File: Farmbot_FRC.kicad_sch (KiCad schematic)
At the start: 0 parts

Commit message: mkb
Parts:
- added J1: XT60-M, XT60-M:AMASS_XT60-M, symbol XT60-M:XT60-M
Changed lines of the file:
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@@
 	(generator_version "9.0")
 	(paper "A4")
+	(symbol
+		(lib_id "XT60-M:XT60-M")
+		(at 59.182 26.162 0)
+		(unit 1)
+		(exclude_from_sim no)
+		(in_bom yes)
+		(on_board yes)
+		(dnp no)
+		(fields_autoplaced yes)
+		(property "Reference" "J1"
+			(at 68.58 23.6219 0)
+			(effects
+				(font
+					(size 1.27 1.27)
+				)
+				(justify left)
+			)
+		)
+		(property "Value" "XT60-M"
+			(at 68.58 26.1619 0)
+			(effects
+				(font
+					(size 1.27 1.27)
+				)
+				(justify left)
+			)
+		)
+		(property "Footprint" "XT60-M:AMASS_XT60-M"
+			(at 59.182 26.162 0)
+			(effects
+				(font
+					(size 1.27 1.27)
+				)
+				(justify bottom)
+				(hide yes)
+			)
+		)
+		(property "Datasheet" ""
+			(at 59.182 26.162 0)
+			(effects
+				(font
+					(size 1.27 1.27)
+				)
+				(hide yes)
+			)
+		)
+		(property "Description" ""
+			(at 59.182 26.162 0)
+			(effects
+				(font
+					(size 1.27 1.27)
+				)
+				(hide yes)
+			)
+		)
+		(property "MF" "AMASS"
+			(at 59.182 26.162 0)
+			(effects
+				(font
+					(size 1.27 1.27)
+				)
+				(justify bottom)
+				(hide yes)
+			)
+		)
+		(property "MAXIMUM_PACKAGE_HEIGHT" "16.00 mm"
+			(at 59.182 26.162 0)
+			(effects
+				(font
+					(size 1.27 1.27)
+				)
+				(justify bottom)
+				(hide yes)
+			)
+		)
+		(property "Package" "Package"
+			(at 59.182 26.162 0)
+			(effects
+				(font
+					(size 1.27 1.27)
+				)
+				(justify bottom)
+				(hide yes)
+			)
+		)
+		(property "Price" "None"
+			(at 59.182 26.162 0)
+			(effects
+				(font
+					(size 1.27 1.27)
+				)
+				(justify bottom)
+				(hide yes)
+			)
+		)
+		(property "Check_prices" "https://www.snapeda.com/parts/XT60-M/AMASS/view-part/?ref=eda"
+			(at 59.182 26.162 0)
+			(effects
+				(font
+					(size 1.27 1.27)
+				)
+				(justify bottom)
+				(hide yes)
+			)
+		)
+		(property "STANDARD" "IPC 7351B"
+			(at 59.182 26.162 0)
+			(effects
+				(font
+					(size 1.27 1.27)
+				)
+				(justify bottom)
+				(hide yes)
+			)
+		)
+		(property "PARTREV" "V1.2"
+			(at 59.182 26.162 0)
+			(effects
+				(font
+					(size 1.27 1.27)
+				)
+				(justify bottom)
+				(hide yes)
+			)
+		)
+		(property "SnapEDA_Link" "https://www.snapeda.com/parts/XT60-M/AMASS/view-part/?ref=snap"
+			(at 59.182 26.162 0)
+			(effects
+				(font
+					(size 1.27 1.27)
+				)
+				(justify bottom)
+				(hide yes)
+			)
+		)
+		(property "MP" "XT60-M"
+			(at 59.182 26.162 0)
+			(effects
+				(font
+					(size 1.27 1.27)
+				)
+				(justify bottom)
+				(hide yes)
+			)
+		)
+		(property "Description_1" "Plug; DC supply; XT60; male; PIN: 2; for cable; soldered; 30A; 500V"
+			(at 59.182 26.162 0)
+			(effects
+				(font
+					(size 1.27 1.27)
+				)
+				(justify bottom)
+				(hide yes)
+			)
+		)
+		(property "Availability" "Not in stock"
+			(at 59.182 26.162 0)
+			(effects
+				(font
+					(size 1.27 1.27)
+				)
+				(justify bottom)
+				(hide yes)
+			)
+		)
+		(property "MANUFACTURER" "AMASS"
+			(at 59.182 26.162 0)
+			(effects
+				(font
+					(size 1.27 1.27)
+				)
+				(justify bottom)
+				(hide yes)
+			)
+		)
+		(pin "P"
+		)
+		(pin "N"
+		)
+		(instances
+			(project ""
+				(path "/c45fa9ee-2918-4f46-896e-3838974ce73e"
+					(reference "J1")
+					(unit 1)
+				)
+			)
+		)
+	)
 	(sheet_instances
 		(path "/"

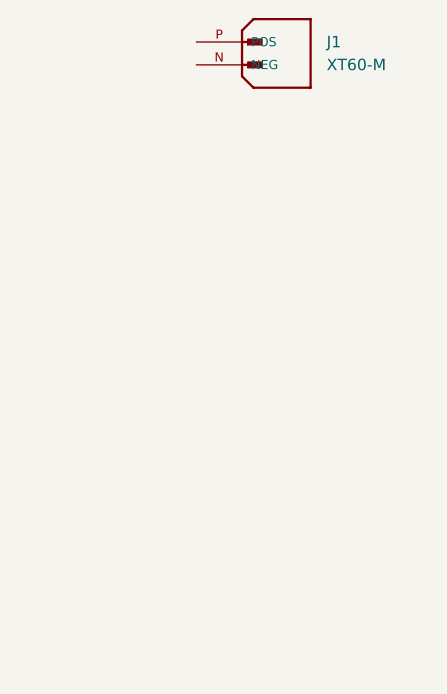
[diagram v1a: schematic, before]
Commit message: added rpi zero
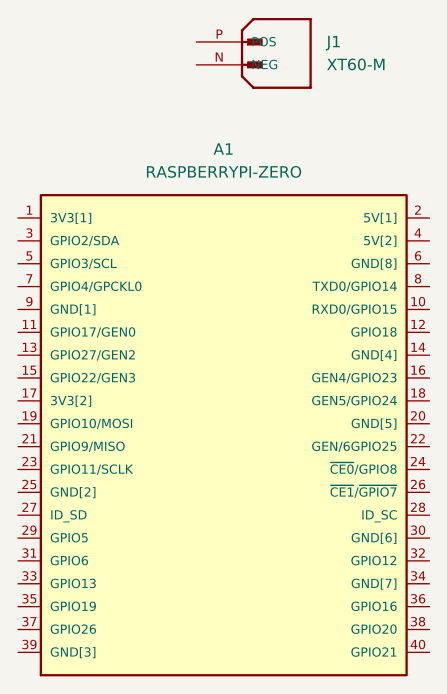
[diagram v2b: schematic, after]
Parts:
- added A1: RASPBERRYPI-ZERO, RASPBERRYPI-ZERO:RASPBERRYPI-ZERO_RPI-ZERO, symbol RASPBERRYPI-ZERO:RASPBERRYPI-ZERO

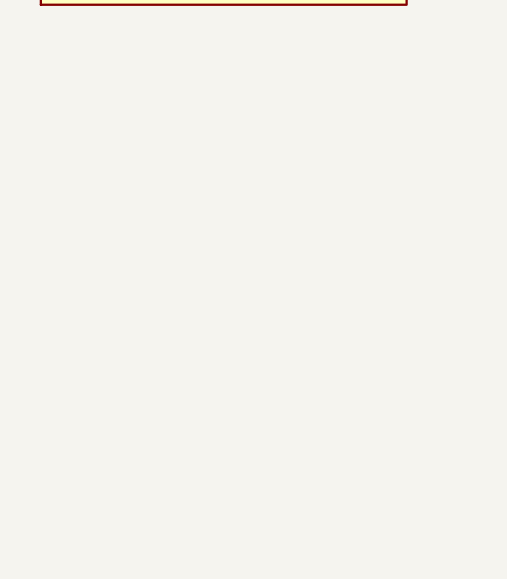
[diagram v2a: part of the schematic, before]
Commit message: added neo6m module
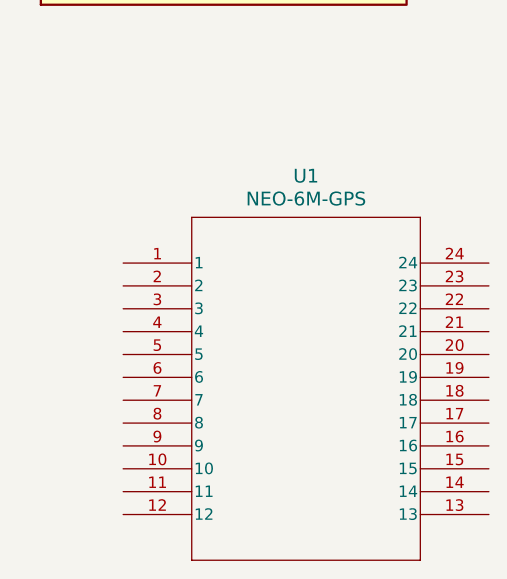
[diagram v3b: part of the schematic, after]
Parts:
- added U1: NEO-6M-GPS, SON_6M-GPS_UBL, symbol gps neo 6m:NEO-6M-GPS
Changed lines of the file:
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@@
 	(paper "A4")
+	(symbol
+		(lib_id "gps neo 6m:NEO-6M-GPS")
+		(at 45.974 122.682 0)
+		(unit 1)
+		(exclude_from_sim no)
+		(in_bom yes)
+		(on_board yes)
+		(dnp no)
+		(fields_autoplaced yes)
+		(property "Reference" "U1"
+			(at 66.294 113.03 0)
+			(effects
+				(font
+					(size 1.524 1.524)
+				)
+			)
+		)
+		(property "Value" "NEO-6M-GPS"
+			(at 66.294 115.57 0)
+			(effects
+				(font
+					(size 1.524 1.524)
+				)
+			)
+		)
+		(property "Footprint" "SON_6M-GPS_UBL"
+			(at 45.974 122.682 0)
+			(effects
+				(font
+					(size 1.27 1.27)
+					(italic yes)
+				)
+				(hide yes)
+			)
+		)
+		(property "Datasheet" "NEO-6M-GPS"
+			(at 45.974 122.682 0)
+			(effects
+				(font
+					(size 1.27 1.27)
+					(italic yes)
+				)
+				(hide yes)
+			)
+		)
+		(property "Description" ""
+			(at 45.974 122.682 0)
+			(effects
+				(font
+					(size 1.27 1.27)
+				)
+				(hide yes)
+			)
+		)
+		(pin "10"
+		)
+		(pin "24"
+		)
+		(pin "23"
+		)
+		(pin "3"
+		)
+		(pin "12"
+		)
+		(pin "15"
+		)
+		(pin "13"
+		)
+		(pin "6"
+		)
+		(pin "22"
+		)
+		(pin "20"
+		)
+		(pin "1"
+		)
+		(pin "2"
+		)
+		(pin "4"
+		)
+		(pin "5"
+		)
+		(pin "7"
+		)
+		(pin "8"
+		)
+		(pin "9"
+		)
+		(pin "11"
+		)
+		(pin "21"
+		)
+		(pin "19"
+		)
+		(pin "18"
+		)
+		(pin "17"
+		)
+		(pin "16"
+		)
+		(pin "14"
+		)
+		(instances
+			(project ""
+				(path "/c45fa9ee-2918-4f46-896e-3838974ce73e"
+					(reference "U1")
+					(unit 1)
+				)
+			)
+		)
+	)
 	(symbol
 		(lib_id "XT60-M:XT60-M")

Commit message: Added basic components
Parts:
- removed A1: RASPBERRYPI-ZERO, RASPBERRYPI-ZERO:RASPBERRYPI-ZERO_RPI-ZERO, symbol RASPBERRYPI-ZERO:RASPBERRYPI-ZERO
- removed J1: XT60-M, XT60-M:AMASS_XT60-M, symbol XT60-M:XT60-M
- removed U1: NEO-6M-GPS, SON_6M-GPS_UBL, symbol gps neo 6m:NEO-6M-GPS
- added J1, J2: Conn_01x20_Socket, symbol Connector:Conn_01x20_Socket
- added J10: halleffect2/bwd, symbol Connector:Conn_01x03_Socket
- added J11: halleffect2/fwd, symbol Connector:Conn_01x03_Socket
- added J12: halleffect1/bwd, symbol Connector:Conn_01x03_Socket
- added J13: halleffect1/fwd, symbol Connector:Conn_01x03_Socket
- added J14: JRACK_IN, XT60-M:AMASS_XT60-M, symbol XT60-M:XT60-M
- added J15: Kill_swt, XT60-M:AMASS_XT60-M, symbol XT60-M:XT60-M
- added J16: EXTRA_24V, XT60-M:AMASS_XT60-M, symbol XT60-M:XT60-M
- added J17: FAN, XT60-M:AMASS_XT60-M, symbol XT60-M:XT60-M
- added J18: npk pwr, symbol Connector:Conn_01x02_Socket
- added J19: camservo/pitch, symbol Connector:Conn_01x03_Socket
- added J20: camservo/yaw, symbol Connector:Conn_01x03_Socket
- added J21: BUCK_OUT[ 5V ], XT60-M:AMASS_XT60-M, symbol XT60-M:XT60-M
- added J3: Conn_01x05_Socket, symbol Connector:Conn_01x05_Socket
- added J4: PWR_IN_24V, XT60-M:AMASS_XT60-M, symbol XT60-M:XT60-M
- added J5: BUCK_IN, XT60-M:AMASS_XT60-M, symbol XT60-M:XT60-M
- added J7: Motor_PWR1, XT60-M:AMASS_XT60-M, symbol XT60-M:XT60-M
- added J9: Stepper_PWR, XT60-M:AMASS_XT60-M, symbol XT60-M:XT60-M
- added SW1: SW_SPST, symbol Switch:SW_SPST
- added U1: 4754, 4754:MODULE_4754, symbol 4754:4754
- added U2: MAX485_MODULE_5V_LOGIC_TLL_TO_RS-485_CONVERTER, MAX485_MODULE_5V_LOGIC_TLL_TO_RS-485_CONVERTER:MODULE_MAX485_MODULE_5V_LOGIC_TLL_TO_RS-485_CONVERTER, symbol max rs485(npk):MAX485_MODULE_5V_LOGIC_TLL_TO_RS-485_CONVERTER
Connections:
- new net 24_IN: J15.P (POS), J4.P (POS)
- new net 24_killed_out: J15.N (NEG), J17.P (POS), J5.P (POS), J7.P (POS)
- new net 5V_unkilled: J21.P (POS), SW1.1 (A)
- new net GND: J3.2 (Pin_2), J4.N (NEG)
- new net PPS: J3.4 (Pin_4)
- new net RX: J3.3 (Pin_3)
- new net TX: J3.5 (Pin_5)
- new net VCC: J3.1 (Pin_1)
- new net pwr 5V: J2.19 (Pin_19)

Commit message: made changes to the pcb
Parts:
- added J-Mdd10A1: Conn_01x05_Socket, Connector_JST:JST_EH_B5B-EH-A_1x05_P2.50mm_Vertical, symbol Connector:Conn_01x05_Socket
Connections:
- net pwr 5V is gone; now on net 5V_killed: J2.19 (Pin_19)
- net 24_killed_out: now also J14.P (POS), J16.P (POS), J9.P (POS)
- net GND: now also J14.N (NEG), J16.N (NEG), J17.N (NEG), J19.1 (Pin_1), J20.1 (Pin_1), J21.N (NEG), J5.N (NEG), J7.N (NEG), J9.N (NEG), U2.1 (GND), J-Mdd10A1.5 (Pin_5)
- net 5V_killed: now reaches J20.2 (Pin_2)
- net 5V_killed: now also J19.2 (Pin_2), SW1.2 (B), U2.4 (VCC)
- net Servo_PWM_Pitch: now reaches J20.3 (Pin_3)
- net NPK_RX: now reaches U2.5 (RO)
- net NPK_Control: now reaches U2.6 (RE)
- net NPK_Control: now also U2.7 (DE)
- net NPK_TX: now reaches U2.8 (DI)
- net Servo_PWM_Yaw: now reaches J19.3 (Pin_3)
- new net DIR1: J-Mdd10A1.1 (Pin_1)
- new net DIR2: J-Mdd10A1.3 (Pin_3)
- new net PWM1: J-Mdd10A1.2 (Pin_2)
- new net PWM2: J-Mdd10A1.4 (Pin_4)
- no-connect marks 0 -> 2
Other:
- moved on the sheet: J14, J15, J16, J17, J19, J4, J9, SW1, U1, U2

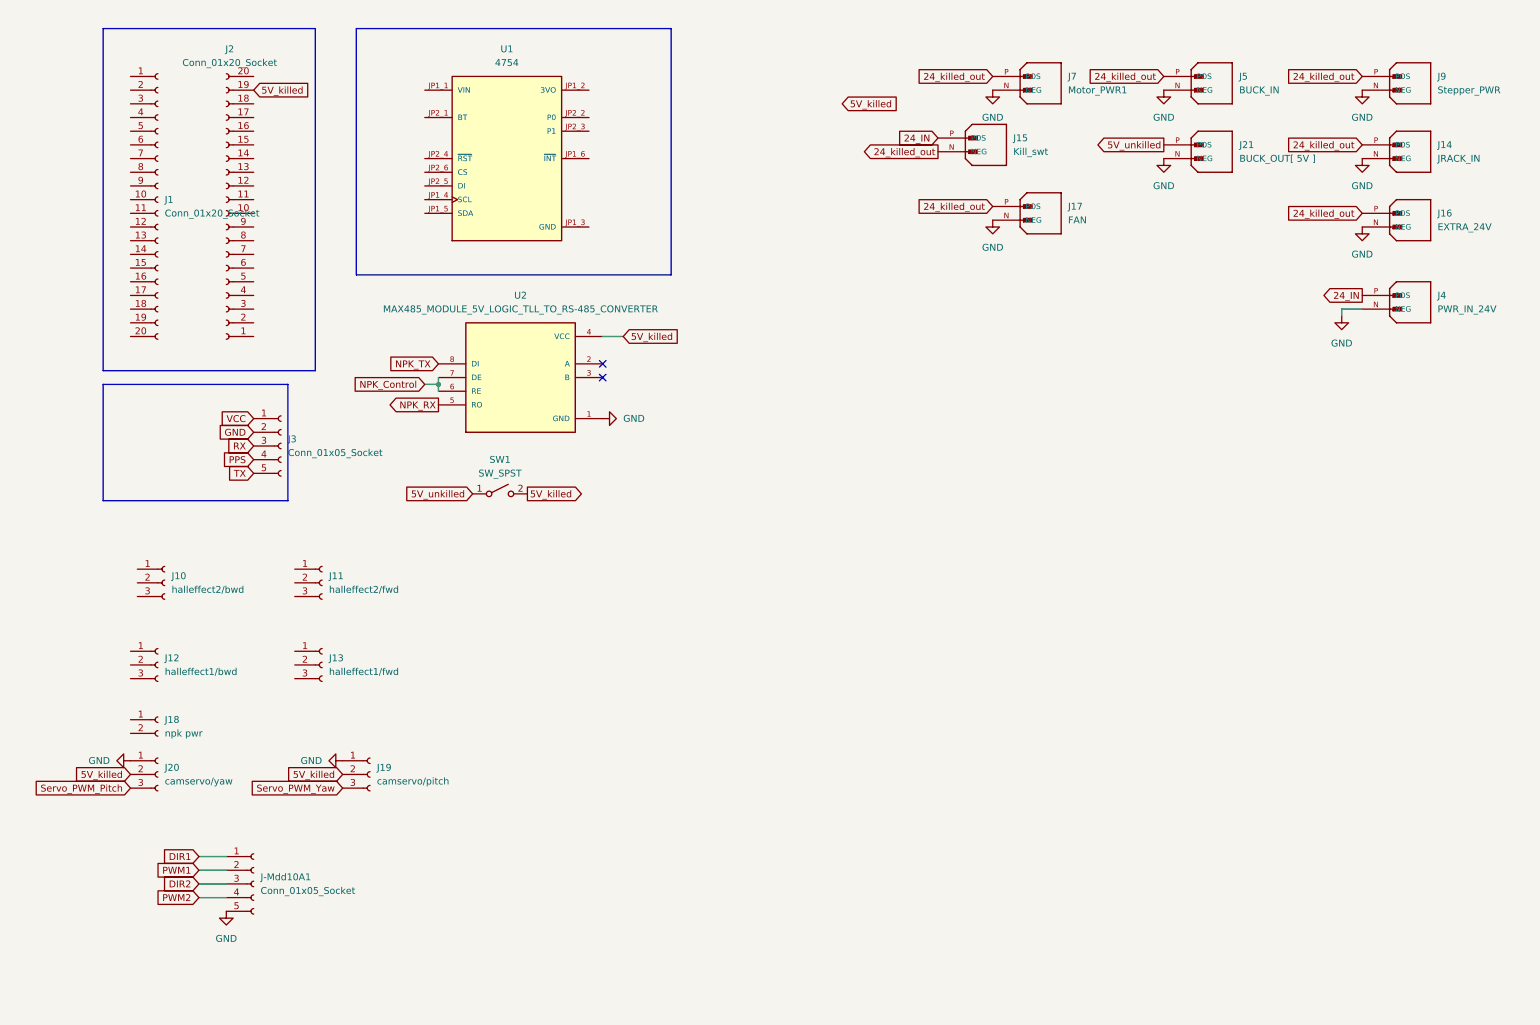
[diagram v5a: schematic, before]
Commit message: made changes to the pcb made most of the communication pins
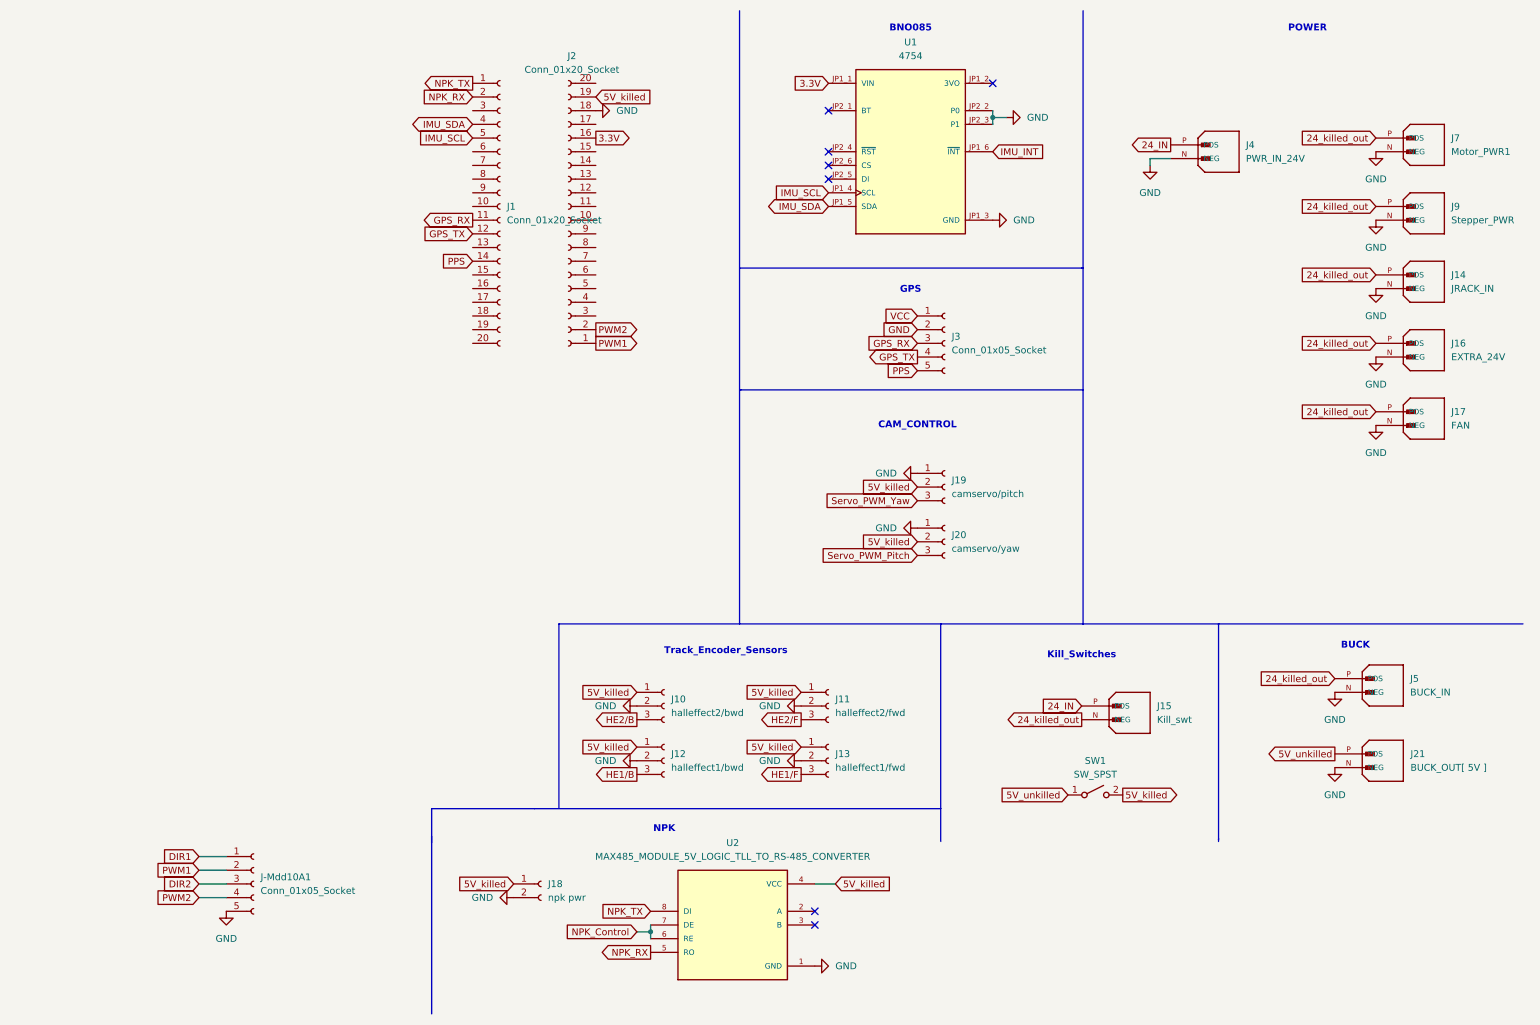
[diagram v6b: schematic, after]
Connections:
- net RX is gone; now on net GPS_RX: J3.3 (Pin_3)
- net TX is gone; now on net PPS: J3.5 (Pin_5)
- net 5V_killed: now also J10.1 (Pin_1), J11.1 (Pin_1), J12.1 (Pin_1), J13.1 (Pin_1), J18.1 (Pin_1)
- net GND: now also J10.2 (Pin_2), J11.2 (Pin_2), J12.2 (Pin_2), J13.2 (Pin_2), J18.2 (Pin_2), J2.18 (Pin_18), U1.JP1_3 (GND), U1.JP2_2 (P0), U1.JP2_3 (P1)
- net NPK_RX: now also J1.2 (Pin_2)
- net NPK_TX: now also J1.1 (Pin_1)
- net PPS: now also J1.14 (Pin_14); no longer J3.4 (Pin_4)
- net PWM1: now also J2.1 (Pin_1)
- net PWM2: now also J2.2 (Pin_2)
- net HE1/B: now reaches J12.3 (Pin_3)
- net HE2/F: now reaches J11.3 (Pin_3)
- net 3.3V: now reaches J2.16 (Pin_16)
- net 3.3V: now also U1.JP1_1 (VIN)
- net GPS_RX: now reaches J1.11 (Pin_11)
- net GPS_TX: now reaches J1.12 (Pin_12)
- net GPS_TX: now also J3.4 (Pin_4)
- net IMU_SDA: now reaches J1.4 (Pin_4)
- net IMU_SDA: now also U1.JP1_5 (SDA)
- net IMU_SCL: now reaches J1.5 (Pin_5)
- net IMU_SCL: now also U1.JP1_4 (SCL)
- net IMU_INT: now reaches U1.JP1_6 (~{INT})
- net HE1/F: now reaches J13.3 (Pin_3)
- net HE2/B: now reaches J10.3 (Pin_3)
- no-connect marks 2 -> 7
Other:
- note added: "BNO085"
- note added: "BUCK"
- note added: "CAM_CONTROL"
- note added: "GPS"
- note added: "Kill_Switches"
- note added: "NPK"
- note added: "POWER"
- note added: "Track_Encoder_Sensors"
- moved on the sheet: J1, J10, J11, J12, J13, J14, J15, J16, J17, J18, J19, J2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
